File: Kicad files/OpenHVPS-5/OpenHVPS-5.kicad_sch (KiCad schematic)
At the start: 76 parts, among them J1 Conn_01x03_Male, Q1 FQT7N10, Q2 BC846A, Q3 MMDT3906, U1 MAX6008AEUR+T, U2 74HC14, U3 MAX4162, U4 CD14538BM

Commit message: Changed R4 to 10K
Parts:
- H1: footprint TestPoint:TestPoint_Loop_D3.80mm_Drill2.0mm -> TestPoint:TestPoint_Loop_D2.60mm_Drill1.4mm_Beaded
- H2: footprint TestPoint:TestPoint_Loop_D3.80mm_Drill2.0mm -> TestPoint:TestPoint_Loop_D3.50mm_Drill1.4mm_Beaded
- TP1, TP2, TP3, TP4, TP5, TP8, TP9: footprint TestPoint:TestPoint_Pad_1.5x1.5mm -> TestPoint:TestPoint_Pad_1.0x1.0mm
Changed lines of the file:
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@@
       (effects (font (size 1.27 1.27)) (justify left) hide)
     )
-    (property "Footprint" "TestPoint:TestPoint_Pad_1.5x1.5mm" (id 2) (at 45.085 147.32 0)
+    (property "Footprint" "TestPoint:TestPoint_Pad_1.0x1.0mm" (id 2) (at 45.085 147.32 0)
       (effects (font (size 1.27 1.27)) hide)
     )
@@
       (effects (font (size 1.27 1.27)) (justify left) hide)
     )
-    (property "Footprint" "TestPoint:TestPoint_Pad_1.5x1.5mm" (id 2) (at 74.295 103.505 0)
+    (property "Footprint" "TestPoint:TestPoint_Pad_1.0x1.0mm" (id 2) (at 74.295 103.505 0)
       (effects (font (size 1.27 1.27)) hide)
     )
@@
       (effects (font (size 1.27 1.27)) (justify left) hide)
     )
-    (property "Footprint" "TestPoint:TestPoint_Pad_1.5x1.5mm" (id 2) (at 85.09 53.975 0)
+    (property "Footprint" "TestPoint:TestPoint_Pad_1.0x1.0mm" (id 2) (at 85.09 53.975 0)
       (effects (font (size 1.27 1.27)) hide)
     )
@@
       (effects (font (size 1.27 1.27)) (justify left) hide)
     )
-    (property "Footprint" "TestPoint:TestPoint_Pad_1.5x1.5mm" (id 2) (at 109.855 85.09 0)
+    (property "Footprint" "TestPoint:TestPoint_Pad_1.0x1.0mm" (id 2) (at 109.855 85.09 0)
       (effects (font (size 1.27 1.27)) hide)
     )
@@
       (effects (font (size 1.27 1.27)) (justify left) hide)
     )
-    (property "Footprint" "TestPoint:TestPoint_Pad_1.5x1.5mm" (id 2) (at 137.16 74.295 0)
+    (property "Footprint" "TestPoint:TestPoint_Pad_1.0x1.0mm" (id 2) (at 137.16 74.295 0)
       (effects (font (size 1.27 1.27)) hide)
     )
@@
       (effects (font (size 1.27 1.27)) (justify left) hide)
     )
-    (property "Footprint" "TestPoint:TestPoint_Pad_1.5x1.5mm" (id 2) (at 181.61 120.65 0)
+    (property "Footprint" "TestPoint:TestPoint_Pad_1.0x1.0mm" (id 2) (at 181.61 120.65 0)
       (effects (font (size 1.27 1.27)) hide)
     )
@@
       (effects (font (size 1.27 1.27)) (justify left) hide)
     )
-    (property "Footprint" "TestPoint:TestPoint_Pad_1.5x1.5mm" (id 2) (at 262.89 131.445 0)
+    (property "Footprint" "TestPoint:TestPoint_Pad_1.0x1.0mm" (id 2) (at 262.89 131.445 0)
       (effects (font (size 1.27 1.27)) hide)
     )
@@
       (effects (font (size 1.27 1.27)) (justify left))
     )
-    (property "Footprint" "TestPoint:TestPoint_Loop_D3.80mm_Drill2.0mm" (id 2) (at 278.765 111.125 0)
+    (property "Footprint" "TestPoint:TestPoint_Loop_D3.50mm_Drill1.4mm_Beaded" (id 2) (at 278.765 111.125 0)
       (effects (font (size 1.27 1.27)) hide)
     )
@@
       (effects (font (size 1.27 1.27)) (justify left))
     )
-    (property "Footprint" "TestPoint:TestPoint_Loop_D3.80mm_Drill2.0mm" (id 2) (at 278.765 127.635 0)
+    (property "Footprint" "TestPoint:TestPoint_Loop_D2.60mm_Drill1.4mm_Beaded" (id 2) (at 278.765 127.635 0)
       (effects (font (size 1.27 1.27)) hide)
     )
@@
     )
     (path "/5534fd63-59cd-4e2a-9176-13a9cbe98172"
-      (reference "H1") (unit 1) (value "Cathode") (footprint "TestPoint:TestPoint_Loop_D3.80mm_Drill2.0mm")
+      (reference "H1") (unit 1) (value "Cathode") (footprint "TestPoint:TestPoint_Loop_D2.60mm_Drill1.4mm_Beaded")
     )
     (path "/8e6f414f-5055-45b6-9d50-4d4f2e754637"
-      (reference "H2") (unit 1) (value "Anode") (footprint "TestPoint:TestPoint_Loop_D3.80mm_Drill2.0mm")
+      (reference "H2") (unit 1) (value "Anode") (footprint "TestPoint:TestPoint_Loop_D3.50mm_Drill1.4mm_Beaded")
     )
     (path "/cfef5cd8-f134-487a-8cb2-e8668492f6e4"
@@
     )
     (path "/9bc9cc82-b773-49fe-90a2-c105343e24b5"
-      (reference "TP1") (unit 1) (value "TestPoint") (footprint "TestPoint:TestPoint_Pad_1.5x1.5mm")
+      (reference "TP1") (unit 1) (value "TestPoint") (footprint "TestPoint:TestPoint_Pad_1.0x1.0mm")
     )
     (path "/10040789-70ae-4f23-b8e8-d562037e7b54"
-      (reference "TP2") (unit 1) (value "TestPoint") (footprint "TestPoint:TestPoint_Pad_1.5x1.5mm")
+      (reference "TP2") (unit 1) (value "TestPoint") (footprint "TestPoint:TestPoint_Pad_1.0x1.0mm")
     )
     (path "/86c269e4-4102-49f2-bde3-f09970185c56"
-      (reference "TP3") (unit 1) (value "TestPoint") (footprint "TestPoint:TestPoint_Pad_1.5x1.5mm")
+      (reference "TP3") (unit 1) (value "TestPoint") (footprint "TestPoint:TestPoint_Pad_1.0x1.0mm")
     )
     (path "/6a4300d9-0bfc-4da6-9c05-64375c3328b2"
-      (reference "TP4") (unit 1) (value "TestPoint") (footprint "TestPoint:TestPoint_Pad_1.5x1.5mm")
+      (reference "TP4") (unit 1) (value "TestPoint") (footprint "TestPoint:TestPoint_Pad_1.0x1.0mm")
     )
     (path "/2f26d85e-0d2d-4e65-8bf8-d015d060e1dd"
-      (reference "TP5") (unit 1) (value "TestPoint") (footprint "TestPoint:TestPoint_Pad_1.5x1.5mm")
+      (reference "TP5") (unit 1) (value "TestPoint") (footprint "TestPoint:TestPoint_Pad_1.0x1.0mm")
     )
     (path "/fab37ed7-f4f8-4e7a-baf0-0f892e4180aa"
@@
     )
     (path "/50eb88bf-3d65-4e85-b575-0f92e6a2605f"
-      (reference "TP8") (unit 1) (value "TestPoint") (footprint "TestPoint:TestPoint_Pad_1.5x1.5mm")
+      (reference "TP8") (unit 1) (value "TestPoint") (footprint "TestPoint:TestPoint_Pad_1.0x1.0mm")
     )
     (path "/849b0334-03ac-475b-8baf-53acddf7999b"
-      (reference "TP9") (unit 1) (value "TestPoint") (footprint "TestPoint:TestPoint_Pad_1.5x1.5mm")
+      (reference "TP9") (unit 1) (value "TestPoint") (footprint "TestPoint:TestPoint_Pad_1.0x1.0mm")
     )
     (path "/00000000-0000-0000-0000-000060096cc3"

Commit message: Cahnged numbering caps
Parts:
- renumbered C11 to C10, C12 to C11, C13 to C12, C14 to C13, C16 to C14, C17 to C15, C18 to C16, C20 to C17, C21 to C18, C10 to C23, C15 to C24
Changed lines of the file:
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@@
   (symbol (lib_id "Device:C") (at 168.91 145.415 0) (unit 1)
     (in_bom yes) (on_board yes)
-    (property "Reference" "C10" (id 0) (at 171.831 144.2466 0)
+    (property "Reference" "C23" (id 0) (at 171.831 144.247 0)
       (effects (font (size 1.27 1.27)) (justify left))
     )
@@
   (symbol (lib_id "Device:C") (at 170.18 99.695 90) (unit 1)
     (in_bom yes) (on_board yes)
-    (property "Reference" "C11" (id 0) (at 170.18 93.2942 90))
+    (property "Reference" "C10" (id 0) (at 170.18 93.294 90))
     (property "Value" "0.1uF" (id 1) (at 170.18 95.6056 90))
     (property "Footprint" "Capacitor_SMD:C_0805_2012Metric" (id 2) (at 173.99 98.73 0)
@@
   (symbol (lib_id "Device:C") (at 177.8 78.105 90) (unit 1)
     (in_bom yes) (on_board yes)
-    (property "Reference" "C12" (id 0) (at 177.8 71.7042 90))
+    (property "Reference" "C11" (id 0) (at 177.8 71.704 90))
     (property "Value" "0.1uF" (id 1) (at 177.8 74.0156 90))
     (property "Footprint" "Capacitor_SMD:C_0805_2012Metric" (id 2) (at 181.61 77.14 0)
@@
   (symbol (lib_id "Device:C") (at 187.96 99.695 90) (unit 1)
     (in_bom yes) (on_board yes)
-    (property "Reference" "C13" (id 0) (at 187.96 93.2942 90))
+    (property "Reference" "C12" (id 0) (at 187.96 93.294 90))
     (property "Value" "0.1uF" (id 1) (at 187.96 95.6056 90))
     (property "Footprint" "Capacitor_SMD:C_0805_2012Metric" (id 2) (at 191.77 98.73 0)
@@
   (symbol (lib_id "Device:C") (at 195.58 78.105 90) (unit 1)
     (in_bom yes) (on_board yes)
-    (property "Reference" "C14" (id 0) (at 195.58 71.7042 90))
+    (property "Reference" "C13" (id 0) (at 195.58 71.704 90))
     (property "Value" "0.1uF" (id 1) (at 195.58 74.0156 90))
     (property "Footprint" "Capacitor_SMD:C_0805_2012Metric" (id 2) (at 199.39 77.14 0)
@@
   (symbol (lib_id "Device:C") (at 200.66 140.335 0) (unit 1)
     (in_bom yes) (on_board yes)
-    (property "Reference" "C15" (id 0) (at 194.0561 139.1856 0)
+    (property "Reference" "C24" (id 0) (at 194.0561 139.1856 0)
       (effects (font (size 1.27 1.27)) (justify left))
     )
@@
   (symbol (lib_id "Device:C") (at 205.74 99.695 90) (unit 1)
     (in_bom yes) (on_board yes)
-    (property "Reference" "C16" (id 0) (at 205.74 93.2942 90))
+    (property "Reference" "C14" (id 0) (at 205.74 93.294 90))
     (property "Value" "0.1uF" (id 1) (at 205.74 95.6056 90))
     (property "Footprint" "Capacitor_SMD:C_0805_2012Metric" (id 2) (at 209.55 98.73 0)
@@
   (symbol (lib_id "Device:C") (at 213.36 78.105 90) (unit 1)
     (in_bom yes) (on_board yes)
-    (property "Reference" "C17" (id 0) (at 213.36 71.7042 90))
+    (property "Reference" "C15" (id 0) (at 213.36 71.704 90))
     (property "Value" "0.1uF" (id 1) (at 213.36 74.0156 90))
     (property "Footprint" "Capacitor_SMD:C_0805_2012Metric" (id 2) (at 217.17 77.14 0)
@@
   (symbol (lib_id "Device:C") (at 223.52 99.695 90) (unit 1)
     (in_bom yes) (on_board yes)
-    (property "Reference" "C18" (id 0) (at 223.52 93.2942 90))
+    (property "Reference" "C16" (id 0) (at 223.52 93.294 90))
     (property "Value" "0.1uF" (id 1) (at 223.52 95.6056 90))
     (property "Footprint" "Capacitor_SMD:C_0805_2012Metric" (id 2) (at 227.33 98.73 0)
@@
   (symbol (lib_id "Device:C") (at 232.41 78.105 90) (unit 1)
     (in_bom yes) (on_board yes)
-    (property "Reference" "C20" (id 0) (at 232.41 71.7042 90))
+    (property "Reference" "C17" (id 0) (at 232.41 71.704 90))
     (property "Value" "0.1uF" (id 1) (at 232.41 74.0156 90))
     (property "Footprint" "Capacitor_SMD:C_0805_2012Metric" (id 2) (at 236.22 77.14 0)
@@
   (symbol (lib_id "Device:C") (at 241.3 99.695 90) (unit 1)
     (in_bom yes) (on_board yes)
-    (property "Reference" "C21" (id 0) (at 241.3 93.2942 90))
+    (property "Reference" "C18" (id 0) (at 241.3 93.294 90))
     (property "Value" "0.1uF" (id 1) (at 241.3 95.6056 90))
     (property "Footprint" "Capacitor_SMD:C_0805_2012Metric" (id 2) (at 245.11 98.73 0)
@@
       (reference "C9") (unit 1) (value "0.1uF") (footprint "Capacitor_SMD:C_0805_2012Metric")
     )
-    (path "/00000000-0000-0000-0000-0000600c7b21"
-      (reference "C10") (unit 1) (value "1uF") (footprint "Capacitor_SMD:C_0805_2012Metric")
-    )
     (path "/00000000-0000-0000-0000-00005ff7f335"
+      (reference "C10") (unit 1) (value "0.1uF") (footprint "Capacitor_SMD:C_0805_2012Metric")
+    )
+    (path "/00000000-0000-0000-0000-00005ff69d16"
       (reference "C11") (unit 1) (value "0.1uF") (footprint "Capacitor_SMD:C_0805_2012Metric")
     )
-    (path "/00000000-0000-0000-0000-00005ff69d16"
+    (path "/00000000-0000-0000-0000-00005ff7f801"
       (reference "C12") (unit 1) (value "0.1uF") (footprint "Capacitor_SMD:C_0805_2012Metric")
     )
-    (path "/00000000-0000-0000-0000-00005ff7f801"
+    (path "/00000000-0000-0000-0000-00005ff6a25a"
       (reference "C13") (unit 1) (value "0.1uF") (footprint "Capacitor_SMD:C_0805_2012Metric")
     )
-    (path "/00000000-0000-0000-0000-00005ff6a25a"
+    (path "/00000000-0000-0000-0000-00005ff7fc43"
       (reference "C14") (unit 1) (value "0.1uF") (footprint "Capacitor_SMD:C_0805_2012Metric")
     )
-    (path "/834bd735-860c-4b4e-b96c-108ade73f718"
-      (reference "C15") (unit 1) (value "1nF") (footprint "Capacitor_SMD:C_0805_2012Metric")
-    )
-    (path "/00000000-0000-0000-0000-00005ff7fc43"
+    (path "/00000000-0000-0000-0000-00005ff6a662"
+      (reference "C15") (unit 1) (value "0.1uF") (footprint "Capacitor_SMD:C_0805_2012Metric")
+    )
+    (path "/00000000-0000-0000-0000-00005ff80085"
       (reference "C16") (unit 1) (value "0.1uF") (footprint "Capacitor_SMD:C_0805_2012Metric")
     )
-    (path "/00000000-0000-0000-0000-00005ff6a662"
+    (path "/00000000-0000-0000-0000-00005ff6ab63"
       (reference "C17") (unit 1) (value "0.1uF") (footprint "Capacitor_SMD:C_0805_2012Metric")
     )
-    (path "/00000000-0000-0000-0000-00005ff80085"
+    (path "/00000000-0000-0000-0000-00005ff808db"
       (reference "C18") (unit 1) (value "0.1uF") (footprint "Capacitor_SMD:C_0805_2012Metric")
     )
@@
       (reference "C19") (unit 1) (value "0.1uF") (footprint "Capacitor_SMD:C_0805_2012Metric")
     )
-    (path "/00000000-0000-0000-0000-00005ff6ab63"
-      (reference "C20") (unit 1) (value "0.1uF") (footprint "Capacitor_SMD:C_0805_2012Metric")
-    )
-    (path "/00000000-0000-0000-0000-00005ff808db"
-      (reference "C21") (unit 1) (value "0.1uF") (footprint "Capacitor_SMD:C_0805_2012Metric")
-    )
     (path "/743b7e51-503f-44bc-a063-83e91538f340"
       (reference "C22") (unit 1) (value "360pF") (footprint "Capacitor_SMD:C_0805_2012Metric")
     )
+    (path "/00000000-0000-0000-0000-0000600c7b21"
+      (reference "C23") (unit 1) (value "1uF") (footprint "Capacitor_SMD:C_0805_2012Metric")
+    )
+    (path "/834bd735-860c-4b4e-b96c-108ade73f718"
+      (reference "C24") (unit 1) (value "1nF") (footprint "Capacitor_SMD:C_0805_2012Metric")
+    )
     (path "/00000000-0000-0000-0000-0000600ddc6a"

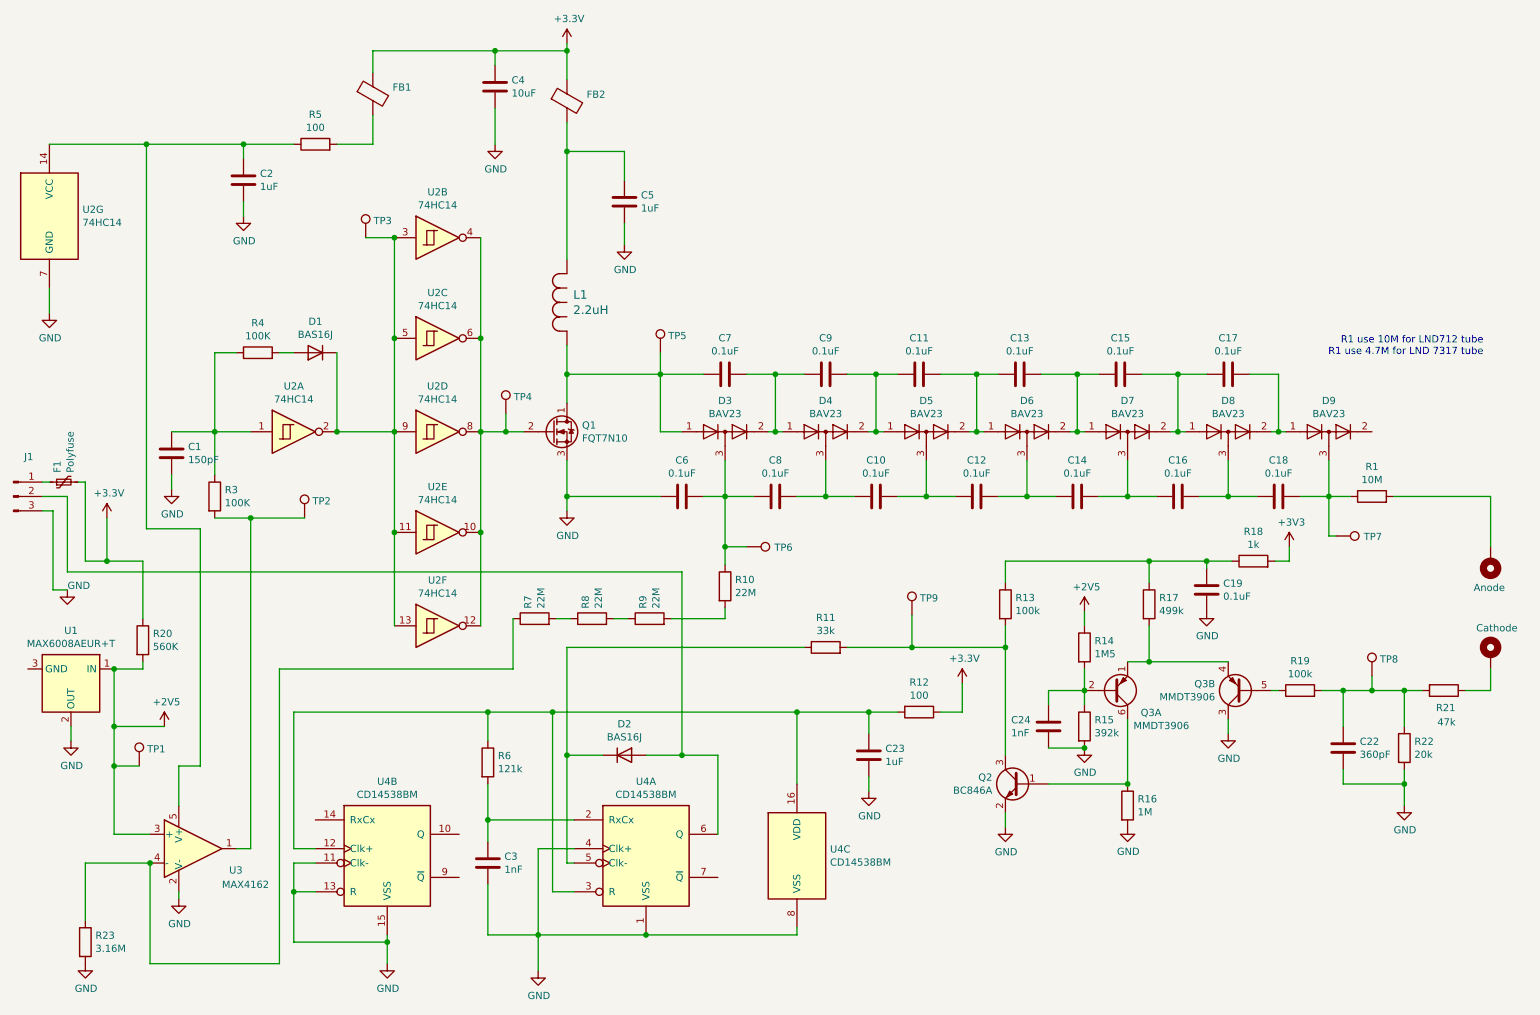
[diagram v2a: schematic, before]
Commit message: fixed missing graphis and  3d model
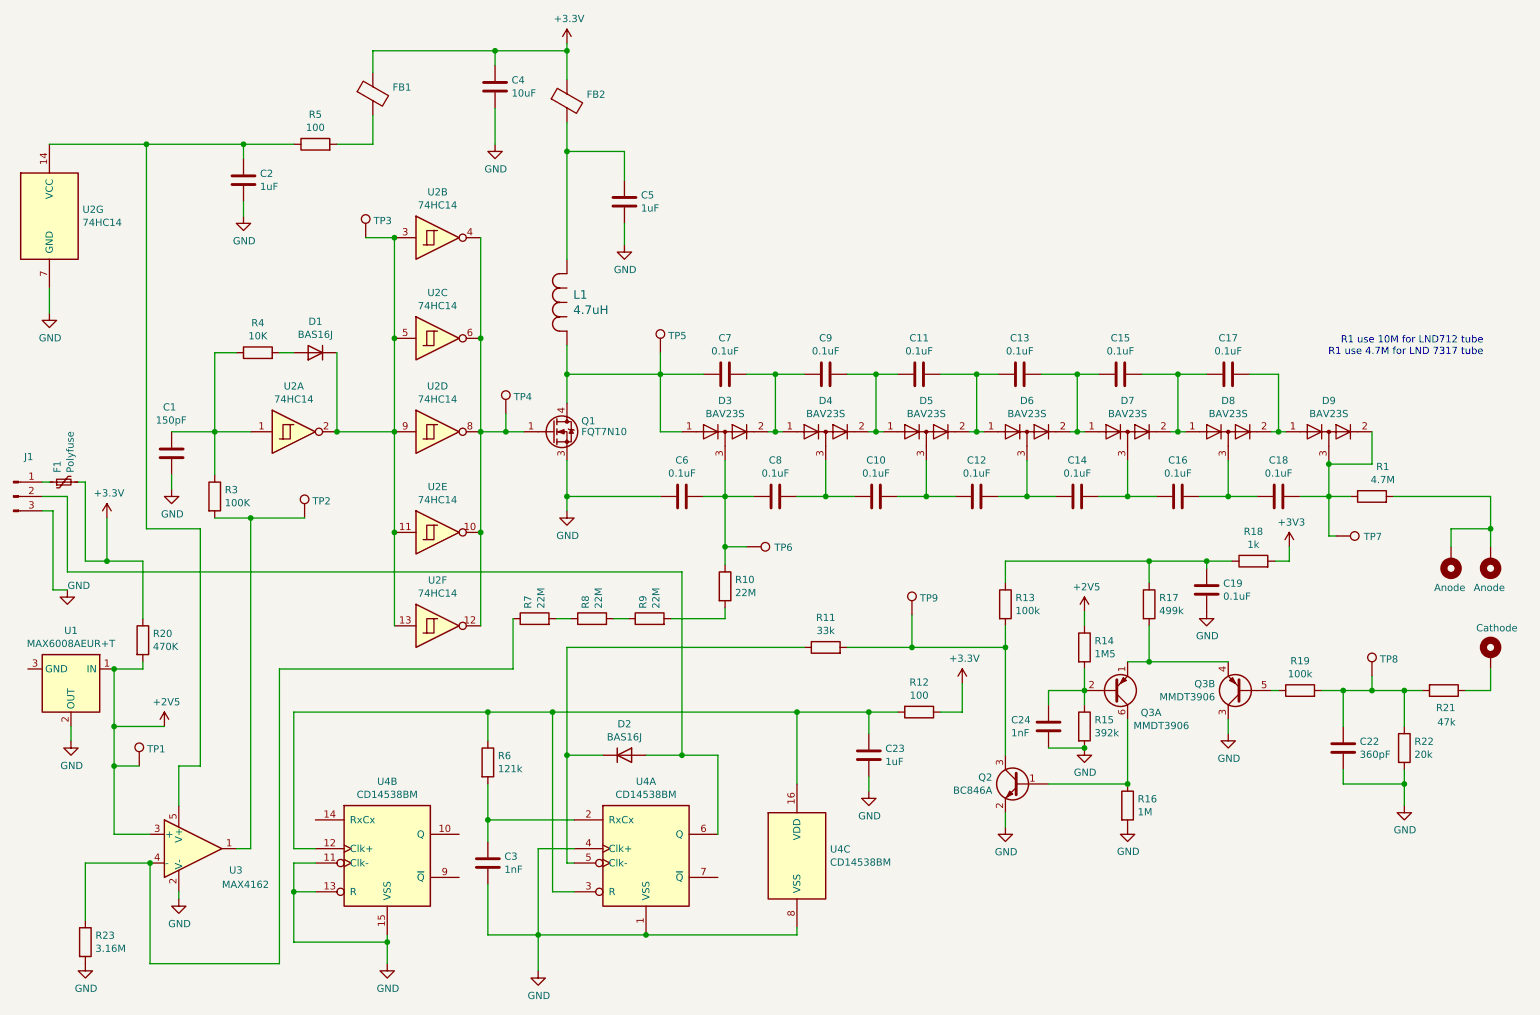
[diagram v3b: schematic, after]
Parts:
- added H4: Anode, TestPoint:TestPoint_Loop_D3.50mm_Drill1.4mm_Beaded, symbol Mechanical:MountingHole_Pad
- D3, D4, D5, D6, D7, D8, D9: value BAV23 -> BAV23S
- L1: value 2.2uH -> 4.7uH
- Q1: footprint Package_TO_SOT_SMD:SOT-223-3_TabPin2 -> Package_TO_SOT_SMD:SOT-223-3_TabPin4
- R1: value 10M -> 4.7M
- R20: value 560K -> 470K
- R4: value 100K -> 10K
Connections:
- net at TP4.1, U2.10, U2.12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: now also Q1.1 (G); no longer Q1.2 (G)
- net at C7.1, D3.1 (K), L1.2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: now also Q1.4 (D); no longer Q1.1 (D)
- net at D9.2 (A): now also C18.2, D9.3 (K), R1.1, TP7.1
- net at H2.1, R1.2: now also H4.1
